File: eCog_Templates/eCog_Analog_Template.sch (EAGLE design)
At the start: 1 part

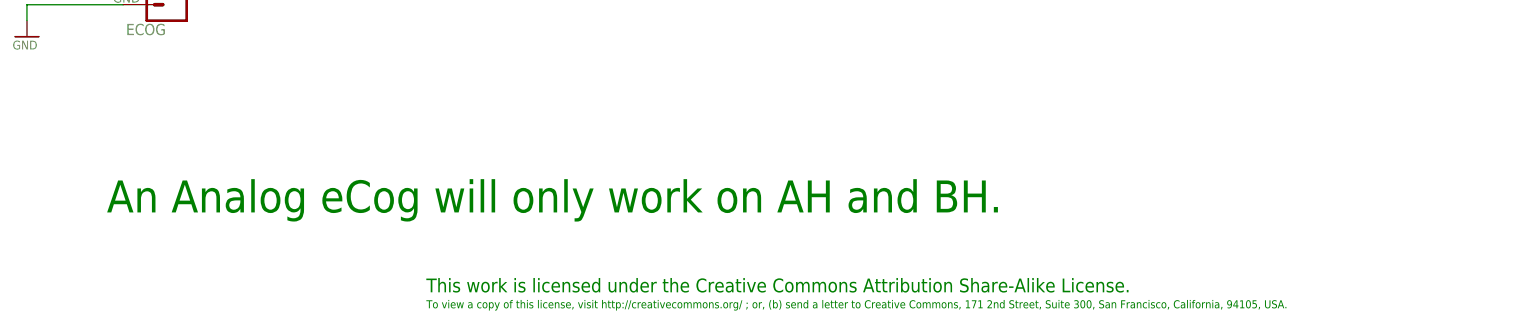
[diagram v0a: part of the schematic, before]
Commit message: Change to through hole and give bette descriptions.
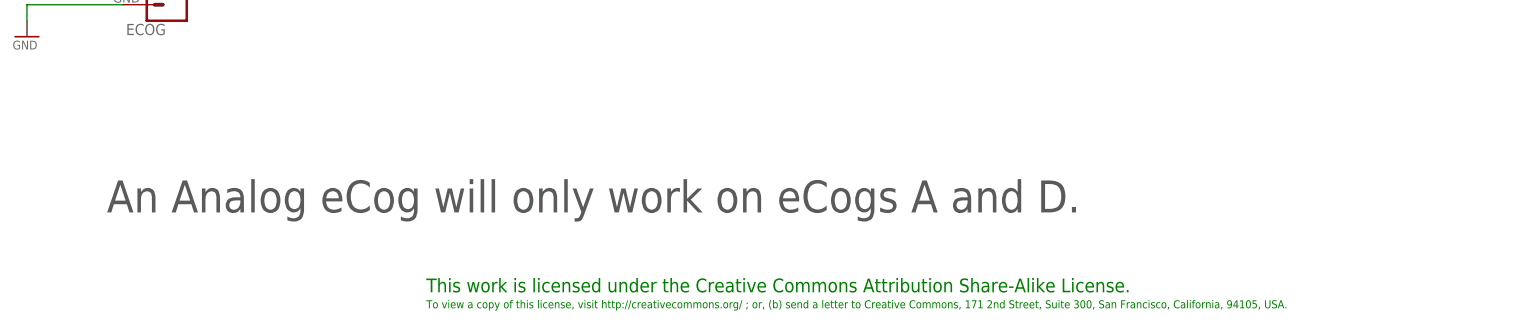
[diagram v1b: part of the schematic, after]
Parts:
- ECOG: value ECOG_GENERAL_ROWECOG_GENERAL_SMD -> ECOG_GENERAL_ROWTHROUGHOLE; device eCogs:ECOG_GENERAL_ROWECOG_GENERAL_SMD -> eCogs:ECOG_GENERAL_ROWTHROUGHOLE
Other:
- note added: "An Analog eCog will only work on eCogs A and D."
- note removed: "An Analog eCog will only work on AH and BH."
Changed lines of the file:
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@@
 <parts>
 <part name="FRAME1" library="frames" deviceset="A3L-LOC" device=""/>
-<part name="ECOG" library="eCogs" deviceset="ECOG_GENERAL_ROW" device="ECOG_GENERAL_SMD" value="ECOG_GENERAL_ROWECOG_GENERAL_SMD"/>
+<part name="ECOG" library="eCogs" deviceset="ECOG_GENERAL_ROW" device="THROUGHOLE" value="ECOG_GENERAL_ROWTHROUGHOLE"/>
 <part name="3V3_PWR1" library="eCogs" deviceset="3V3" device=""/>
 <part name="GND1" library="eCogs" deviceset="GND" device=""/>
@@
 <text x="317.5" y="30.48" size="2.1844" layer="91">Copyright 2016 Gadget Factory, LLC</text>
 <text x="317.5" y="25.4" size="1.778" layer="91">See more details at www.GadgetFactory.net</text>
-<text x="48.26" y="22.86" size="5.08" layer="91">An Analog eCog will only work on AH and BH.</text>
+<text x="48.26" y="22.86" size="5.08" layer="97">An Analog eCog will only work on eCogs A and D.</text>
 </plain>
 <instances>
